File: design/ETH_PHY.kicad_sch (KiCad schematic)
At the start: 45 parts

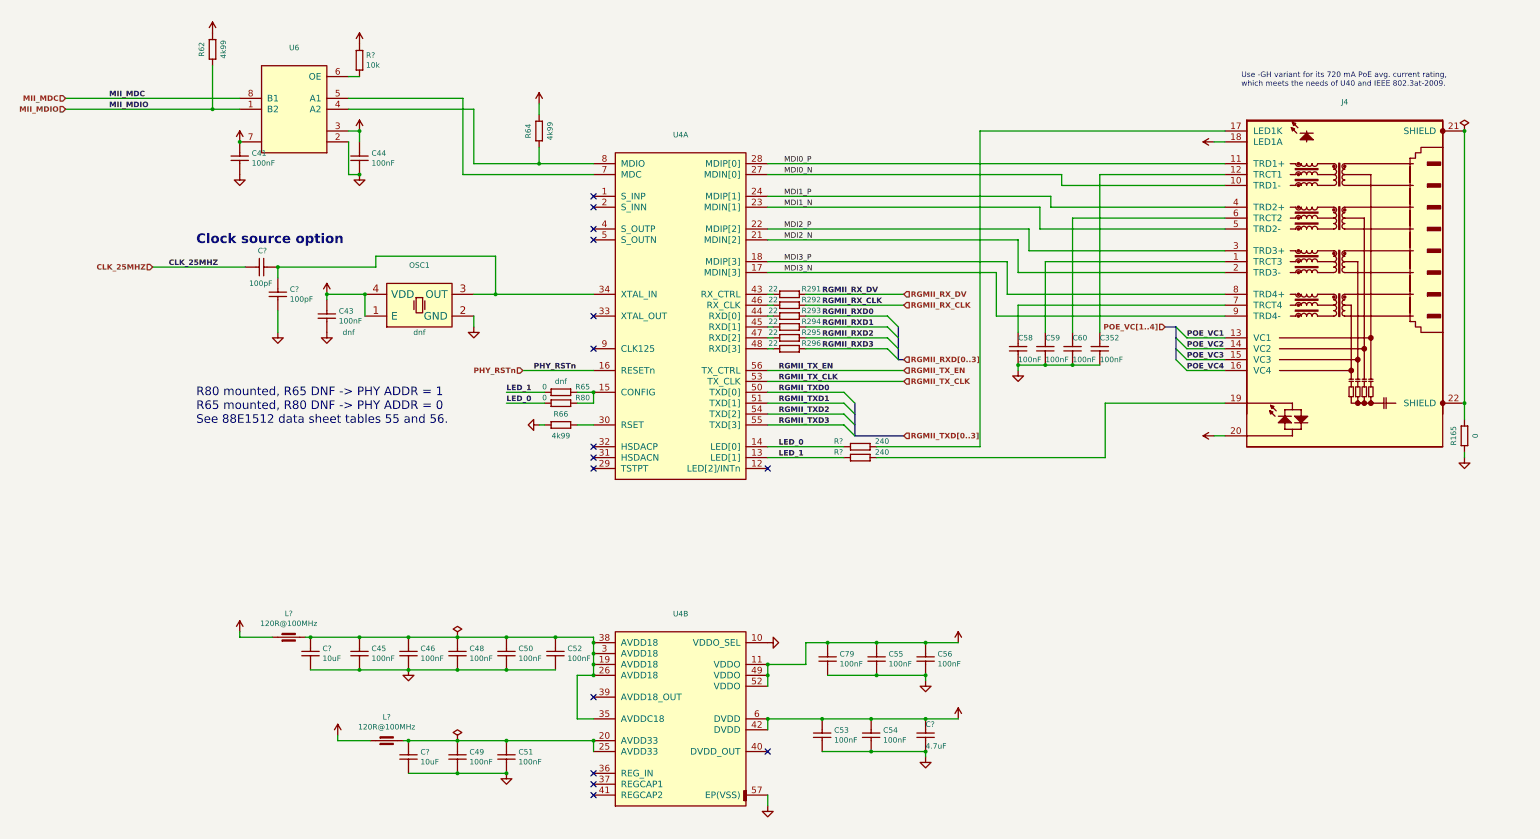
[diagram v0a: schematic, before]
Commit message: new power converter added
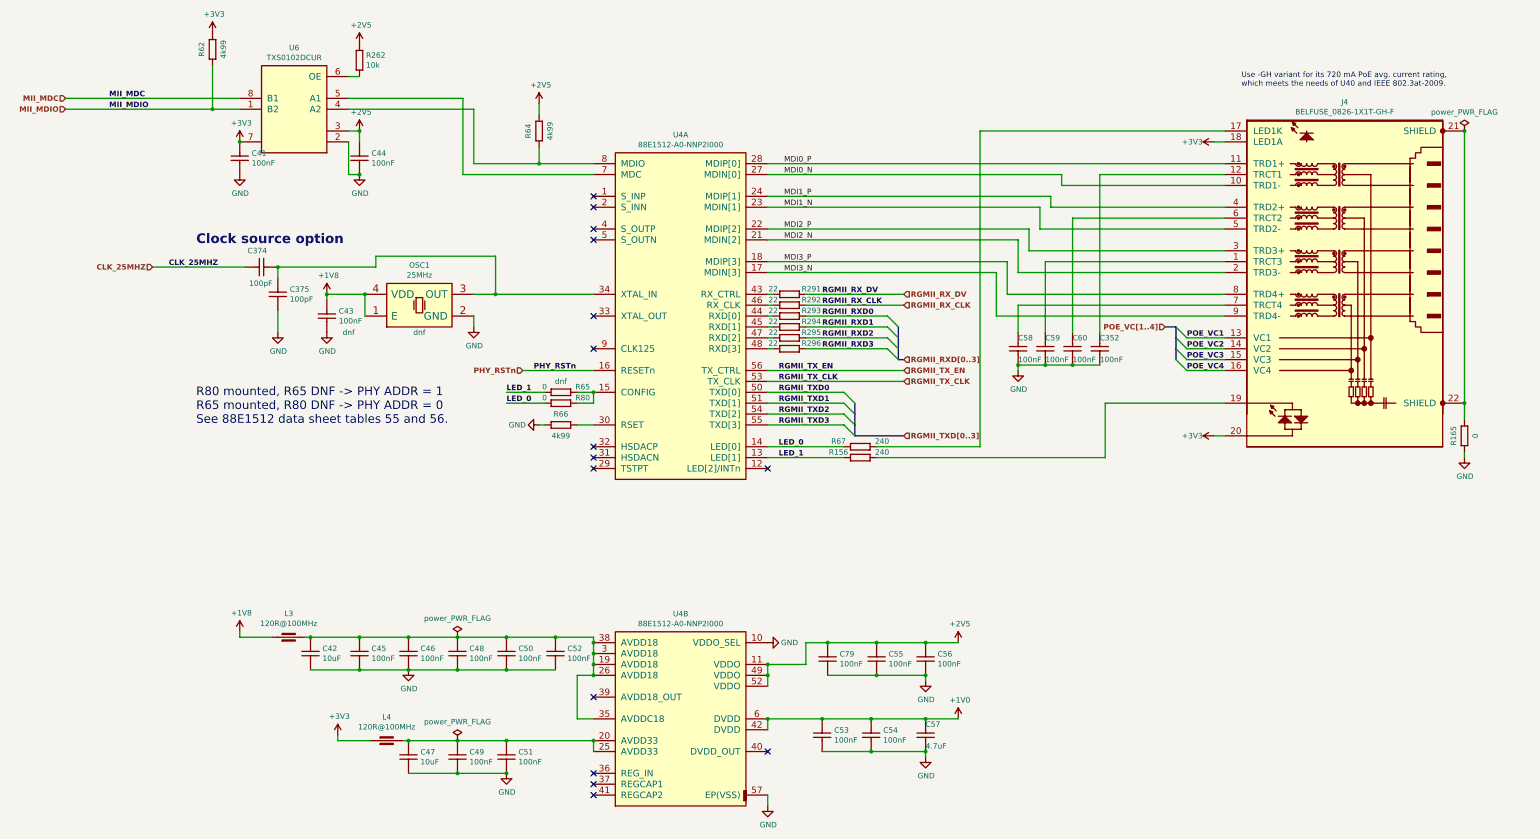
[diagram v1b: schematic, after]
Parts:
- C352, C41, C43, C44, C45, C46, C48, C49, C50, C51, C52, C53, C54, C55, C56, C58, C59, C60, C79: value (none) -> CC0201_100NF_6.3V_10%_X5R; footprint (none) -> CAPC0603X33N
- C374, C375: renamed from C?; value (none) -> CC0402_100PF_50V_5%_C0G; footprint (none) -> Capacitors SMD:CAPC1005X55N
- C42, C47: renamed from C?; value (none) -> CC0603_10UF_6.3V_20%_X5R; footprint (none) -> CAPC1608X87N
- C57: renamed from C?; value (none) -> CC0603_4.7UF_25V_10%_X5R; footprint (none) -> Capacitors SMD:CAPC1608X90N
- J4: value (none) -> BELFUSE_0826-1X1T-GH-F; footprint (none) -> BELFUSE_0826-1X1T-80-F
- L3, L4: renamed from L?; value (none) -> IND0603_MURATA_BLM18SG121TN1D; footprint (none) -> INDC1608X65N
- OSC1: value (none) -> 25MHz; footprint (none) -> ICs And Semiconductors SMD:OSC_MICREL_2520
- R156, R67: renamed from R?; value (none) -> R0402_240R_1%_0.0625W_100PPM; footprint (none) -> Resistors SMD:RESC1005X40N
- R165, R65, R80: value (none) -> R0402_0R_JUMPER; footprint (none) -> RESC1005X40N
- R262: renamed from R?; value (none) -> R0402_10K_1%_0.0625W_100PPM; footprint (none) -> RESC1005X40N
- R291, R292, R293, R294, R295, R296: value (none) -> R0402_22R_1%_0.0625W_100PPM; footprint (none) -> RESC1005X40N
- R62, R64, R66: value (none) -> R0603_4K99_1%_0.063W_50PPM; footprint (none) -> RESC1608X55N
- U4: value (none) -> 88E1512-A0-NNP2I000; footprint (none) -> ICs And Semiconductors SMD:QFN50P800X800X100-57N-S437
- U6: value (none) -> TXS0102DCUR; footprint (none) -> SOP50P310X90-8N

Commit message: connected signals to the J9 connector
connected signals to the J9 connector
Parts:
- C352, C374, C375, C41, C42, C43, C44, C45, C46, C47, C48, C49, C50, C51, C52, C53, C54, C55, C56, C57, C58, C59, C60, C79, J4, L3, L4, R156, R165, R262, R291, R292, R293, R294, R295, R296, R62, R64, R65, R66, R67, R80: Author CERN DEM JLC -> (none)
- U4, U6: Author CERN DEM JLC -> (none); Bonding No -> (none)

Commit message: Attempt to add and improve BOM. Added new part numbers for some of the passives
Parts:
- C42, C47: MANUFACTURER (none) -> GENERIC; MANUFACTURER PART NUMBER (none) -> CC0603_10UF_6.3V_20%_X5R; Manufacturer Part Number CC0603_10uF_6.3V_20%_X5R -> CC0603_10UF_6.3V_20%_X5R
- R165, R65, R80: MANUFACTURER (none) -> GENERIC
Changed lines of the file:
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@@
       (effects (font (size 1.524 1.524)) (justify left) hide)
     )
-    (property "Manufacturer Part Number" "CC0603_10uF_6.3V_20%_X5R" (id 23) (at 155.956 176.53 0)
+    (property "Manufacturer Part Number" "CC0603_10UF_6.3V_20%_X5R" (id 23) (at 155.956 176.53 0)
       (effects (font (size 1.524 1.524)) (justify left) hide)
     )
@@
       (effects (font (size 1.524 1.524)) (justify left) hide)
     )
+    (property "MANUFACTURER" "GENERIC" (id 40) (at 99.06 176.53 0)
+      (effects (font (size 1.27 1.27)) hide)
+    )
+    (property "MANUFACTURER PART NUMBER" "CC0603_10UF_6.3V_20%_X5R" (id 41) (at 99.06 176.53 0)
+      (effects (font (size 1.27 1.27)) hide)
+    )
     (pin "1")
     (pin "2")
@@
       (effects (font (size 1.524 1.524)) (justify left) hide)
     )
-    (property "Manufacturer Part Number" "CC0603_10uF_6.3V_20%_X5R" (id 23) (at 178.816 200.66 0)
+    (property "Manufacturer Part Number" "CC0603_10UF_6.3V_20%_X5R" (id 23) (at 178.816 200.66 0)
       (effects (font (size 1.524 1.524)) (justify left) hide)
     )
@@
       (effects (font (size 1.524 1.524)) (justify left) hide)
     )
+    (property "MANUFACTURER" "GENERIC" (id 40) (at 121.92 200.66 0)
+      (effects (font (size 1.27 1.27)) hide)
+    )
+    (property "MANUFACTURER PART NUMBER" "CC0603_10UF_6.3V_20%_X5R" (id 41) (at 121.92 200.66 0)
+      (effects (font (size 1.27 1.27)) hide)
+    )
     (pin "1")
     (pin "2")
@@
     )
     (property "config" "dnf" (id 41) (at 157.48 109.22 0))
+    (property "MANUFACTURER" "GENERIC" (id 42) (at 153.67 111.76 0)
+      (effects (font (size 1.27 1.27)) hide)
+    )
     (pin "1")
     (pin "2")
@@
       (effects (font (size 1.524 1.524)) (justify left) hide)
     )
+    (property "MANUFACTURER" "GENERIC" (id 41) (at 368.3 125.73 0)
+      (effects (font (size 1.27 1.27)) hide)
+    )
     (pin "1")
     (pin "2")
@@
       (effects (font (size 1.524 1.524)) (justify left) hide)
     )
+    (property "MANUFACTURER" "GENERIC" (id 41) (at 153.67 114.3 0)
+      (effects (font (size 1.27 1.27)) hide)
+    )
     (pin "1")

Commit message: Restore some consistency in schematic metadata
Still 13 problematic footprint names in LTM4673.kicad_sch:

BAD Dup: "Footprint" "CAPC1608X87N" "Capacitors SMD:CAPC1005X55N" in LTM4673-altium-import:0_Capacitor - non polarized
BAD Dup: "Footprint" "CAPC2012X135N" "CAPC1608X87N" in LTM4673-altium-import:1_Capacitor - non polarized
BAD Dup: "Footprint" "CAPC1608X87N" "Capacitors SMD:CAPC1005X55N" in LTM4673-altium-import:1_Capacitor - non polarized
BAD Dup: "Footprint" "CAPC3216X180N" "CAPC3225X270N" in LTM4673-altium-import:1_Capacitor - non polarized
BAD Dup: "Footprint" "CAPC1608X87N" "Capacitors SMD:CAPC1005X55N" in LTM4673-altium-import:0_Capacitor - non polarized
BAD Dup: "Footprint" "CAPC1608X87N" "Capacitors SMD:CAPC1005X55N" in LTM4673-altium-import:0_Capacitor - non polarized
BAD Dup: "Footprint" "CAPC3216X180N" "CAPC3225X270N" in LTM4673-altium-import:1_Capacitor - non polarized
BAD Dup: "Footprint" "CAPC2012X135N" "CAPC1608X87N" in LTM4673-altium-import:1_Capacitor - non polarized
BAD Dup: "Footprint" "CAPC3216X180N" "CAPC3225X270N" in LTM4673-altium-import:1_Capacitor - non polarized
BAD Dup: "Footprint" "CAPC1608X87N" "Capacitors SMD:CAPC1005X55N" in LTM4673-altium-import:0_Capacitor - non polarized
BAD Dup: "Footprint" "CAPC1608X87N" "Capacitors SMD:CAPC1005X55N" in LTM4673-altium-import:1_Capacitor - non polarized
BAD Dup: "Footprint" "CAPC3216X180N" "CAPC3225X270N" in LTM4673-altium-import:1_Capacitor - non polarized
BAD Dup: "Footprint" "CAPMP7343X310N" "Capacitor_Tantalum_SMD:CP_EIA-7343-30_AVX-N" in LTM4673-altium-import:3_Capacitor - polarized

But the Symbol Field editor in eeschema should be more useful now.
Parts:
- C42, C47: MANUFACTURER GENERIC -> (none); MANUFACTURER PART NUMBER CC0603_10UF_6.3V_20%_X5R -> (none)
- R165, R65, R80: MANUFACTURER GENERIC -> (none)
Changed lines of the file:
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@@
       (effects (font (size 1.524 1.524)) (justify left) hide)
     )
-    (property "MANUFACTURER" "GENERIC" (id 40) (at 99.06 176.53 0)
-      (effects (font (size 1.27 1.27)) hide)
-    )
-    (property "MANUFACTURER PART NUMBER" "CC0603_10UF_6.3V_20%_X5R" (id 41) (at 99.06 176.53 0)
-      (effects (font (size 1.27 1.27)) hide)
-    )
     (pin "1")
     (pin "2")
@@
       (effects (font (size 1.524 1.524)) (justify left) hide)
     )
-    (property "MANUFACTURER" "GENERIC" (id 40) (at 121.92 200.66 0)
-      (effects (font (size 1.27 1.27)) hide)
-    )
-    (property "MANUFACTURER PART NUMBER" "CC0603_10UF_6.3V_20%_X5R" (id 41) (at 121.92 200.66 0)
-      (effects (font (size 1.27 1.27)) hide)
-    )
     (pin "1")
     (pin "2")
@@
     )
     (property "config" "dnf" (id 41) (at 157.48 109.22 0))
-    (property "MANUFACTURER" "GENERIC" (id 42) (at 153.67 111.76 0)
-      (effects (font (size 1.27 1.27)) hide)
-    )
     (pin "1")
     (pin "2")
@@
       (effects (font (size 1.524 1.524)) (justify left) hide)
     )
-    (property "MANUFACTURER" "GENERIC" (id 41) (at 368.3 125.73 0)
-      (effects (font (size 1.27 1.27)) hide)
-    )
     (pin "1")
     (pin "2")
@@
       (effects (font (size 1.524 1.524)) (justify left) hide)
     )
-    (property "MANUFACTURER" "GENERIC" (id 41) (at 153.67 114.3 0)
-      (effects (font (size 1.27 1.27)) hide)
-    )
     (pin "1")
